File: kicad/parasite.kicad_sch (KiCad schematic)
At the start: 29 parts, among them Q1 MMBT3906, Q4 Q_Photo_NPN, SW1 B3U-1000P, U1 E73-2G4M08S1C, U2 SHTC3, Y1 32.768kHz

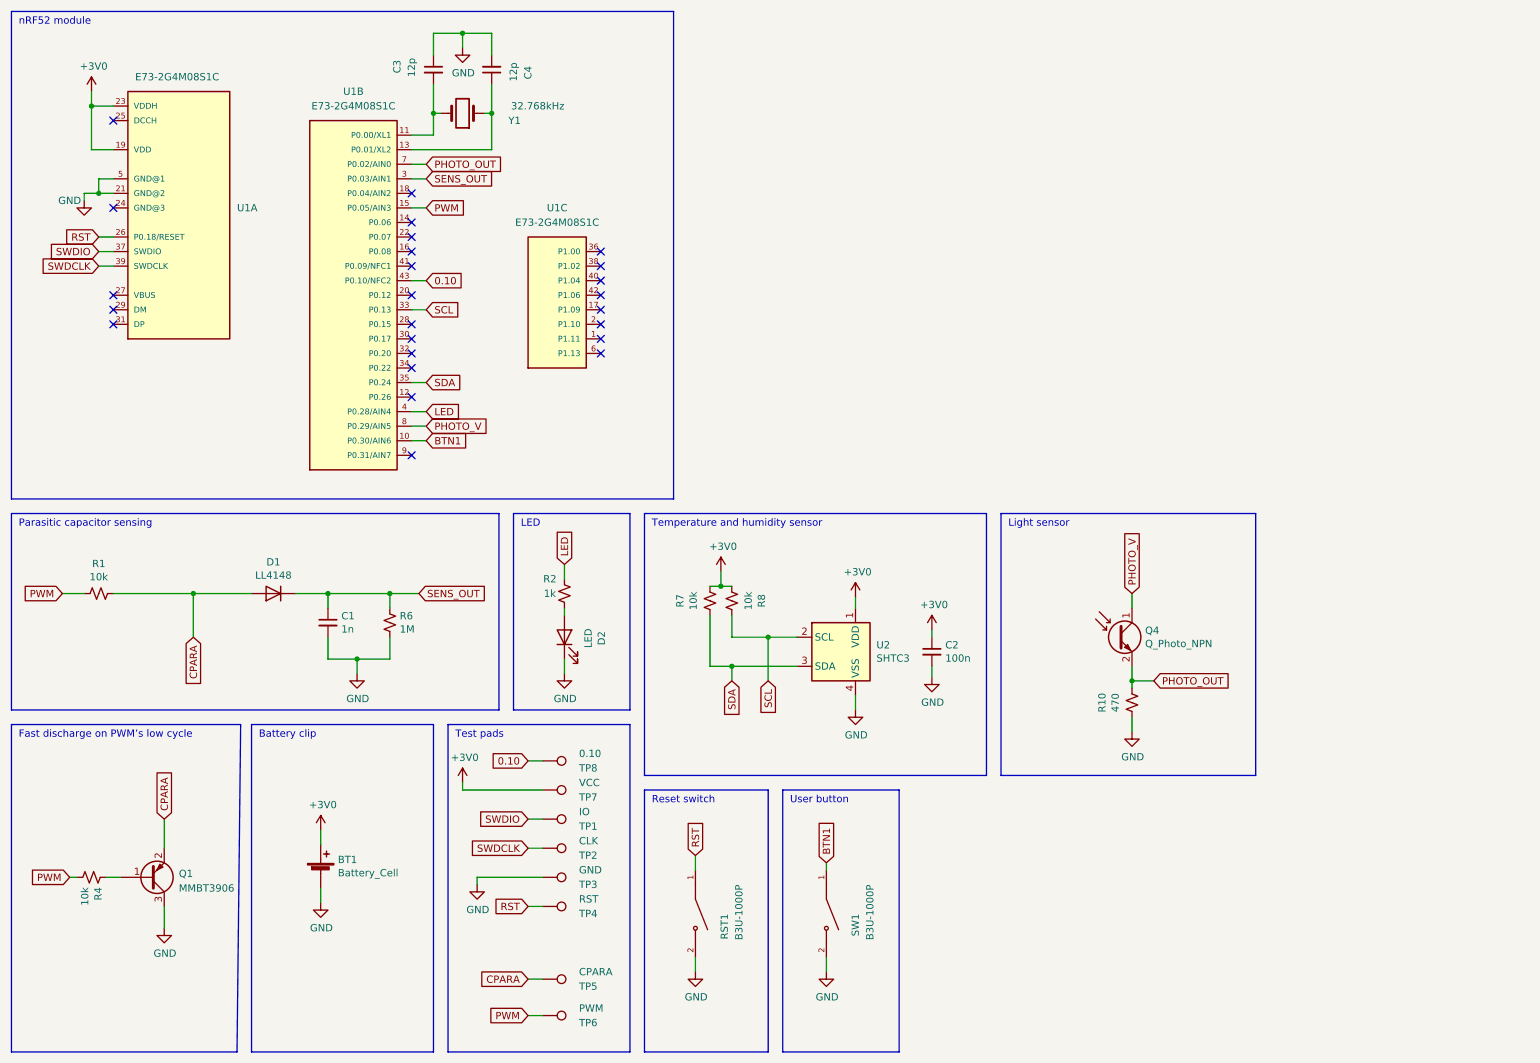
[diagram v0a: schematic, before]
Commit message: Update Schematic to add 2 more sense points
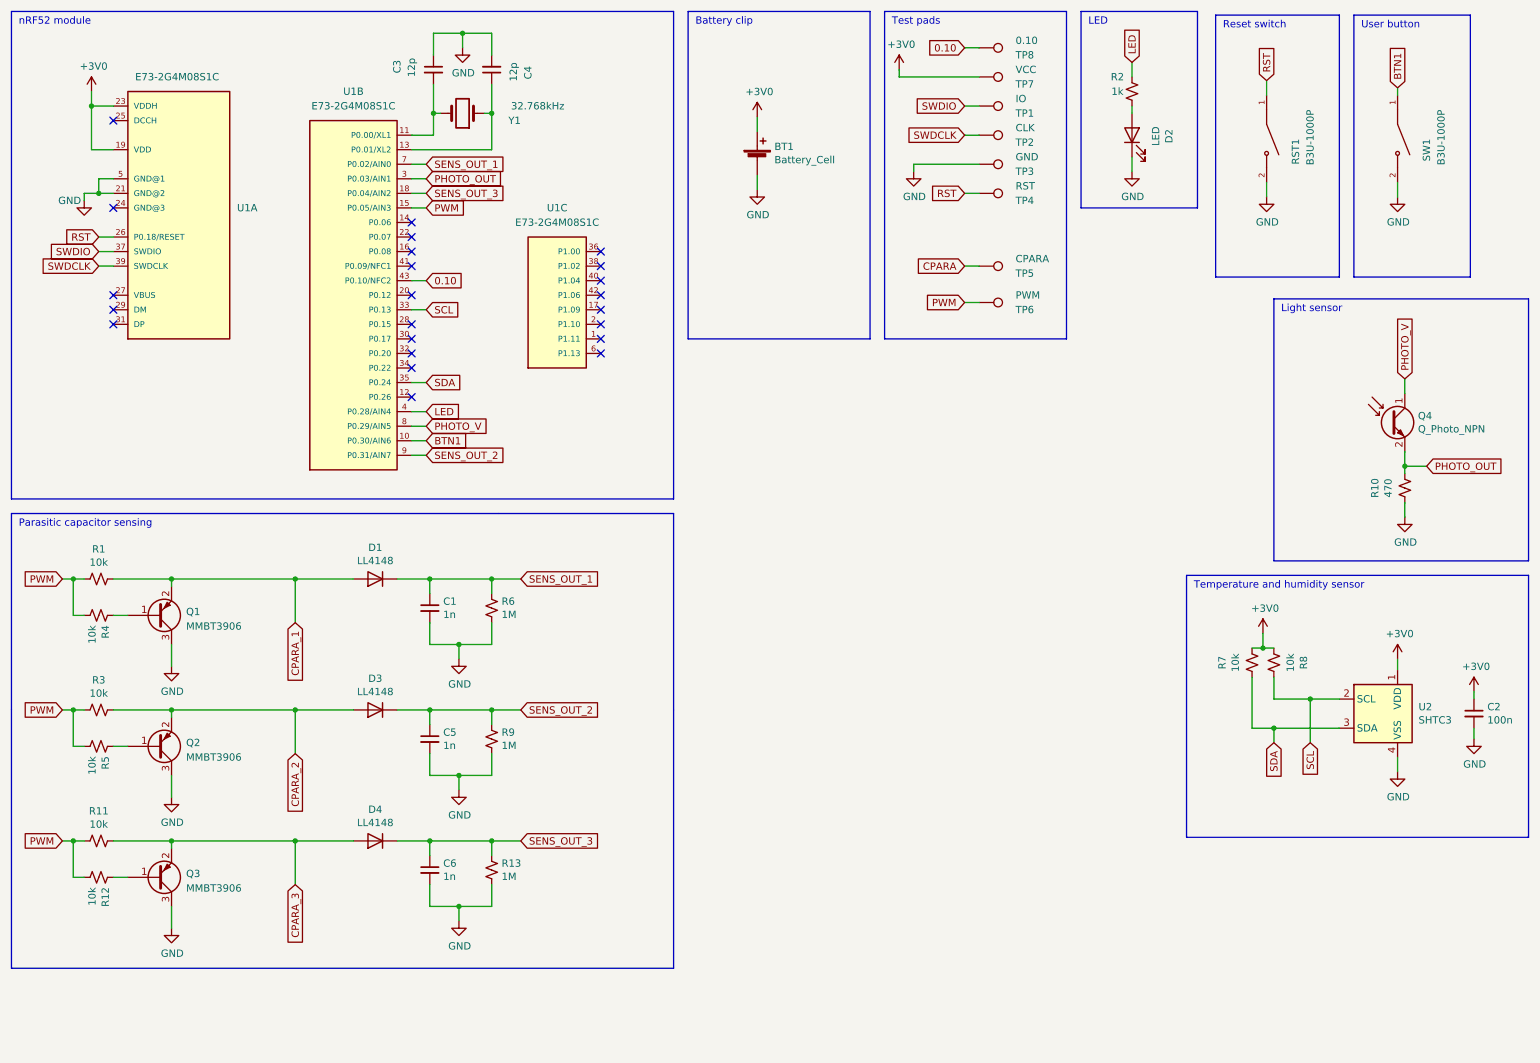
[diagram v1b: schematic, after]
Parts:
- added C5, C6: 1n, Capacitor_SMD:C_0402_1005Metric, symbol Device:C_Small
- added D3, D4: LL4148, Diode_SMD:D_MiniMELF, symbol Diode:LL4148
- added Q2, Q3: MMBT3906, Package_TO_SOT_SMD:SOT-23, symbol Transistor_BJT:MMBT3906
- added R11, R12, R3, R5: 10k, Resistor_SMD:R_0402_1005Metric, symbol Device:R_Small_US
- added R13, R9: 1M, Resistor_SMD:R_0402_1005Metric, symbol Device:R_Small_US
- RST1, SW1: footprint SW_B3U-1000P -> snapeda:SW_B3U-1000P
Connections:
- net CPARA: no longer D1.2 (A), Q1.2 (E), R1.2
- net GND: now also C5.2, C6.2, Q2.3 (C), Q3.3 (C), R13.2, R9.2
- net PHOTO_OUT: now also U1.3 (P0.03/AIN1); no longer U1.7 (P0.02/AIN0)
- net PWM: now also R11.1, R12.2, R3.1, R5.2
- net SENS_OUT_3: now reaches U1.18 (P0.04/AIN2)
- net SENS_OUT_3: now also C6.1, D4.1 (K), R13.1
- net SENS_OUT_2: now reaches U1.9 (P0.31/AIN7)
- net SENS_OUT_2: now also C5.1, D3.1 (K), R9.1
- net SENS_OUT renamed SENS_OUT_1
- net SENS_OUT_1: now also U1.7 (P0.02/AIN0); no longer U1.3 (P0.03/AIN1)
- new net: Q2.1 (B), R5.1
- new net: Q3.1 (B), R12.1
- new net CPARA_1: D1.2 (A), Q1.2 (E), R1.2
- new net CPARA_2: D3.2 (A), Q2.2 (E), R3.2
- new net CPARA_3: D4.2 (A), Q3.2 (E), R11.2
- no-connect marks 25 -> 23
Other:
- note removed: "Fast discharge on PWM’s low cycle"
- moved on the sheet: BT1, C1, C2, D1, D2, Q1, Q4, R1, R10, R2, R4, R6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

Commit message: updated PCB with 3 zones and soil temp sensor
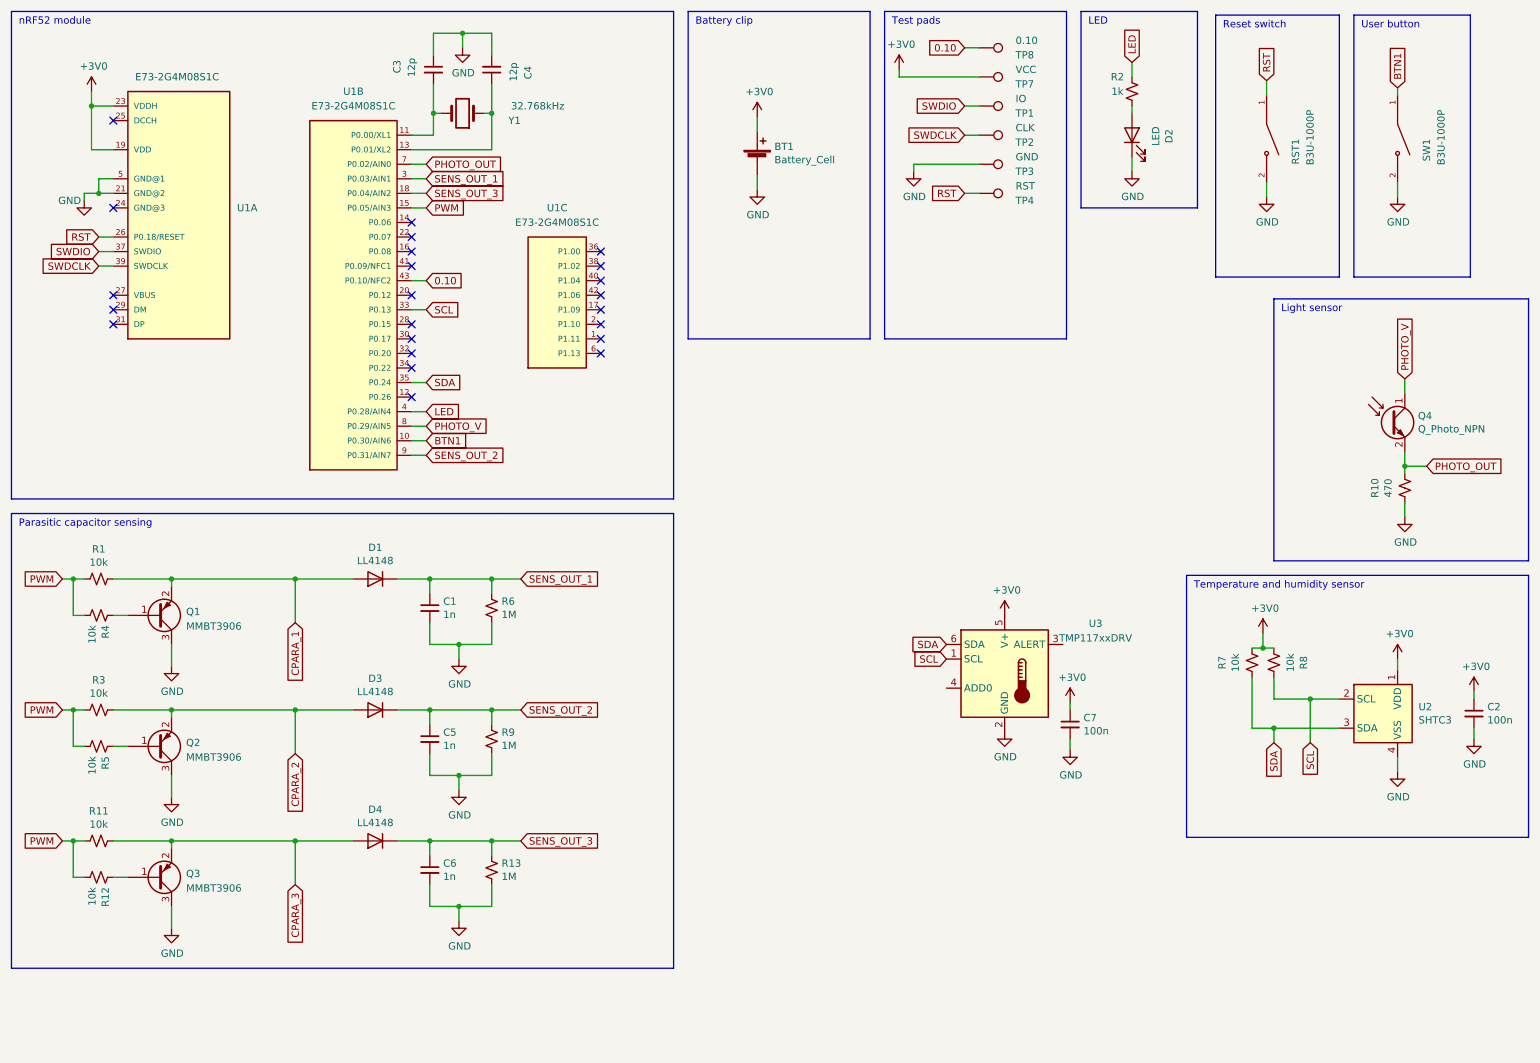
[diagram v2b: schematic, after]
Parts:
- removed TP5: CPARA, TestPoint:TestPoint_Pad_D1.0mm, symbol Connector:TestPoint
- removed TP6: PWM, TestPoint:TestPoint_Pad_D1.0mm, symbol Connector:TestPoint
- added C7: 100n, Capacitor_SMD:C_0402_1005Metric, symbol Device:C_Small
- added U3: TMP117xxDRV, Package_SON:WSON-6-1EP_2x2mm_P0.65mm_EP1x1.6mm, symbol Sensor_Temperature:TMP117xxDRV
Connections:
- net +3V0: now also C7.1, U3.5 (V+)
- net GND: now also C7.2, U3.2 (GND)
- net PHOTO_OUT: now also U1.7 (P0.02/AIN0); no longer U1.3 (P0.03/AIN1)
- net SCL: now also U3.1 (SCL)
- net SDA: now also U3.6 (SDA)
- net SENS_OUT_1: now also U1.3 (P0.03/AIN1); no longer U1.7 (P0.02/AIN0)

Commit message: added lcsc part numbers and a temp sensor
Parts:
- U3: LCSC (none) -> C2803242
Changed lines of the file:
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@@
       (effects (font (size 1.27 1.27)) (justify left) hide)
+    )
+    (property "LCSC" "C2803242" (at 191.135 129.54 0)
+      (effects (font (size 1.27 1.27)) hide)
     )
     (pin "1")

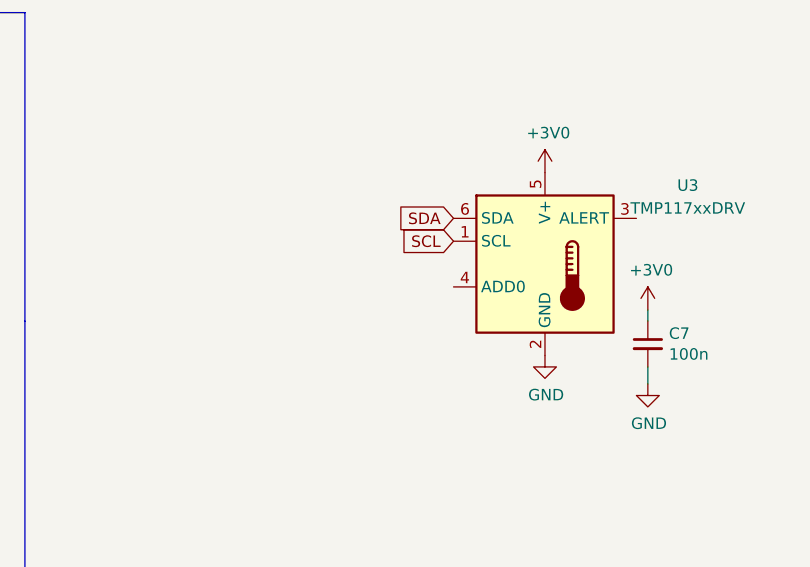
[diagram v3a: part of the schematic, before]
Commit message: Fixed i2c address pin issue
Connected pin to 3v to program 0x49 address
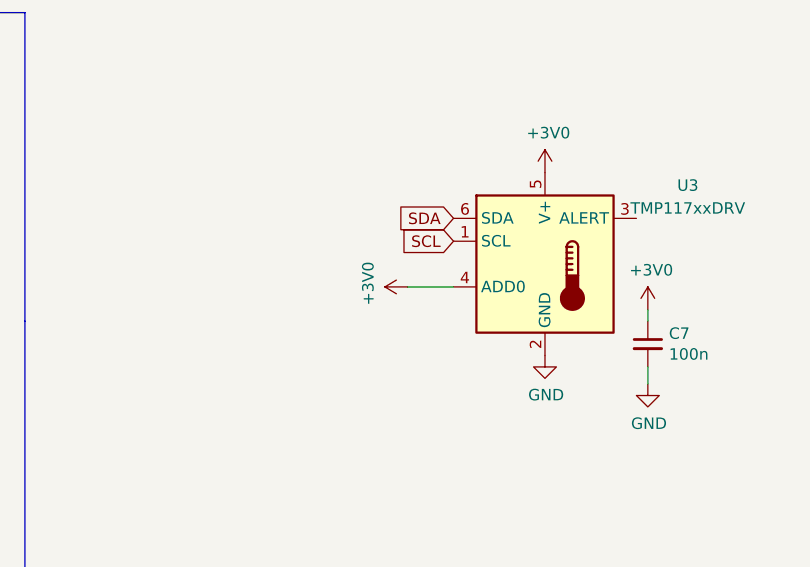
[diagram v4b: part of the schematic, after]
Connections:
- net +3V0: now also U3.4 (ADD0)
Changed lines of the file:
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@@
+    (stroke (width 0) (type default))
+  )
+  (wire (pts (xy 175.895 132.08) (xy 180.975 132.08))
     (stroke (width 0) (type default))
   )
@@
         )
       )
+    )
+  )
+  (symbol (lib_id "power:+3V0") (at 175.895 132.08 90) (unit 1)
+    (in_bom yes) (on_board yes) (dnp no)
+    (property "Reference" "#PWR010" (at 179.705 132.08 0)
+      (effects (font (size 1.27 1.27)) hide)
+    )
+    (property "Value" "+3V0" (at 171.5008 131.699 0)
+      (effects (font (size 1.27 1.27)))
+    )
+    (property "Footprint" "" (at 175.895 132.08 0)
+      (effects (font (size 1.27 1.27)) hide)
+    )
+    (property "Datasheet" "" (at 175.895 132.08 0)
+      (effects (font (size 1.27 1.27)) hide)
+    )
+    (pin "1")
+    (instances
+      (project "parasite"
+        (path "/922058ca-d09a-45fd-8394-05f3e2c1e03a"
+          (reference "#PWR010") (unit 1)
+        )
+      )
